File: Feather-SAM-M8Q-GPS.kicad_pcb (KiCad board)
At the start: 2 copper layers, 50.8 x 22.9 mm, 37 parts, among them U1 ublox_SAM-M8Q

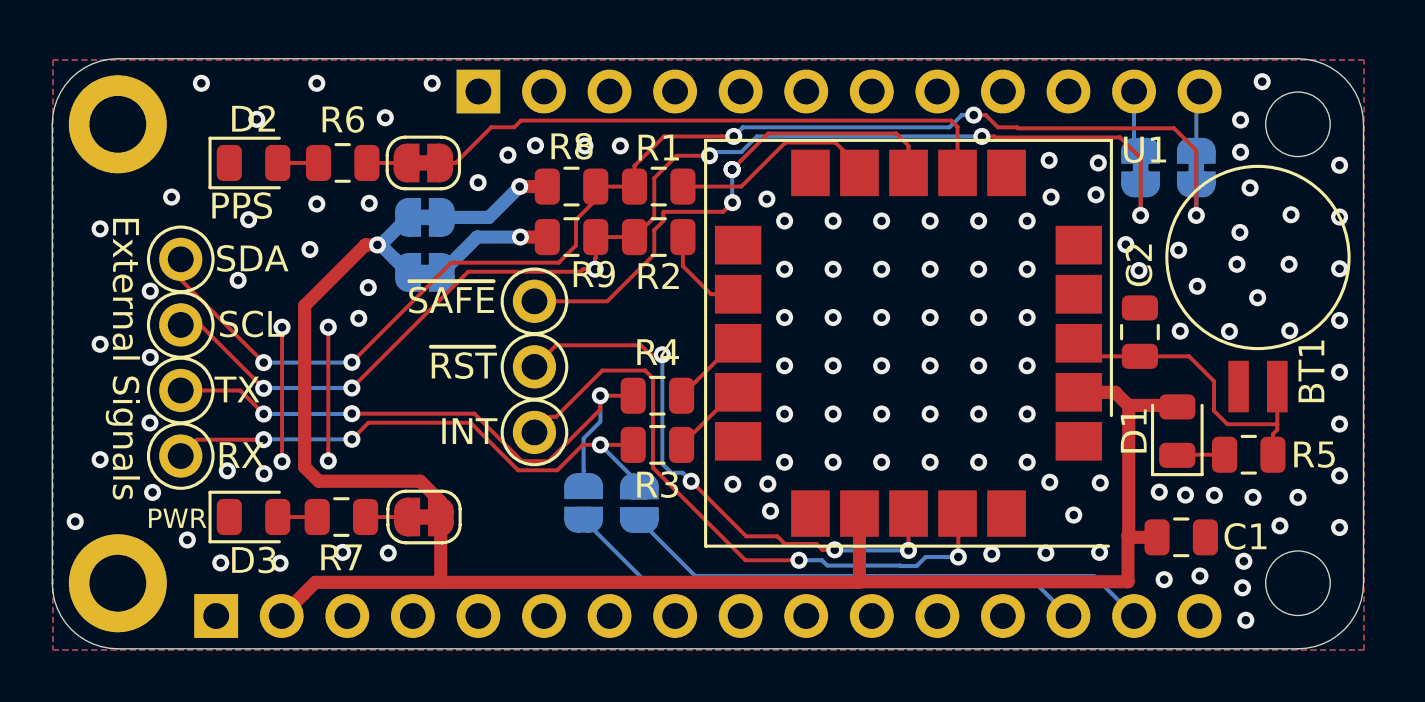
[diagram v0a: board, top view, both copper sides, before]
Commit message: Rev1.5 of SAM-M8Q GPS
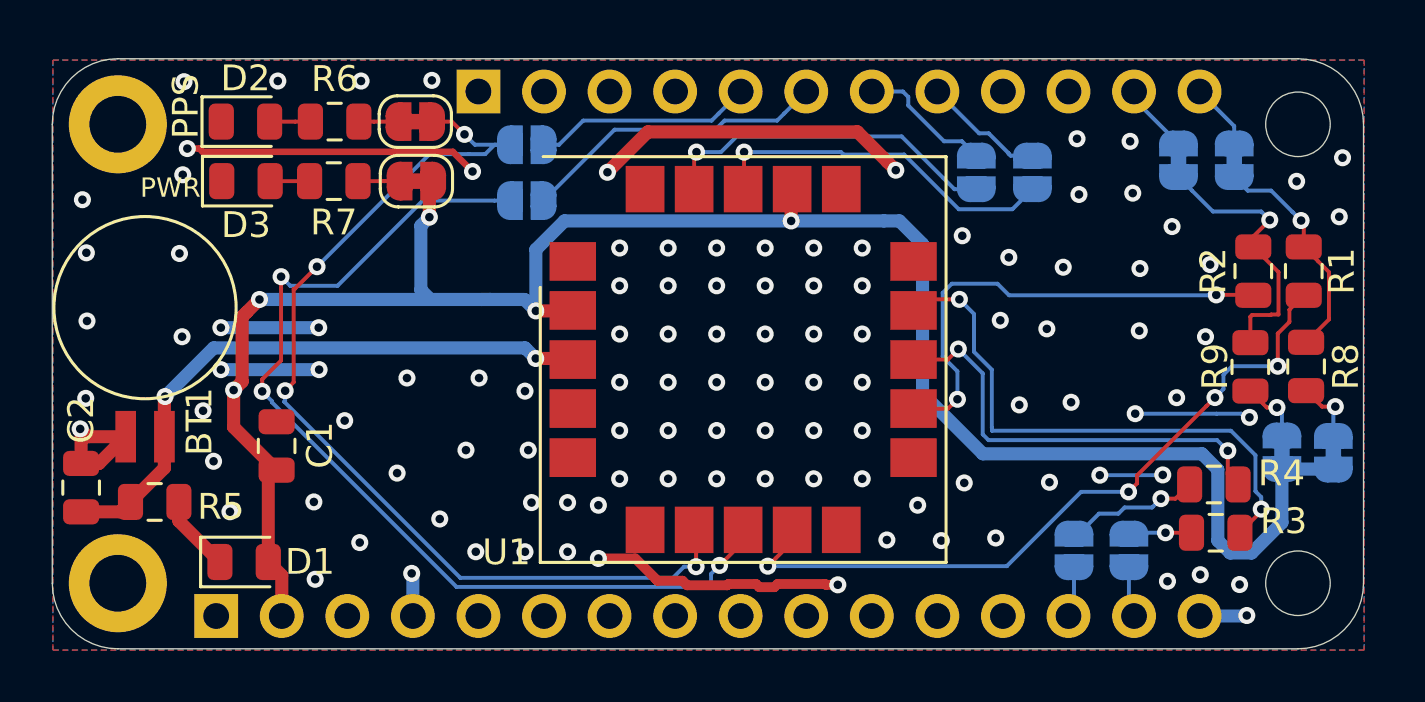
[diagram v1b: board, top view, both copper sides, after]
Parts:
- removed RX1: RX, Connector_Pin:Pin_D1.0mm_L10.0mm
- removed RX2: SCL, Connector_Pin:Pin_D1.0mm_L10.0mm
- removed RX3: INT, Connector_Pin:Pin_D1.0mm_L10.0mm
- removed TX1: TX, Connector_Pin:Pin_D1.0mm_L10.0mm
- removed TX2: SDA, Connector_Pin:Pin_D1.0mm_L10.0mm
- removed TX3: ~SAFE, Connector_Pin:Pin_D1.0mm_L10.0mm
- removed TX4: ~RST, Connector_Pin:Pin_D1.0mm_L10.0mm
- added JP10: ~, Jumper:SolderJumper-2_P1.3mm_Open_RoundedPad1.0x1.5mm, B.Cu at (122.1, 60.2)
- added JP11: ~, Jumper:SolderJumper-2_P1.3mm_Open_RoundedPad1.0x1.5mm, B.Cu at (124.3, 60.2)
- added JP12: ~, Jumper:SolderJumper-2_P1.3mm_Open_RoundedPad1.0x1.5mm, B.Cu at (104.7, 59.2)
- added JP9: ~, Jumper:SolderJumper-2_P1.3mm_Open_RoundedPad1.0x1.5mm, B.Cu at (104.7, 61.3)
- moved BT1 43.2 mm to (89.9, 70.5)
- moved R5 42.4 mm to (90.3, 73.0), turned to 0 degrees
- moved C2 41.5 mm to (87.5, 72.4)
- moved D1 36.5 mm to (93.8, 75.3), turned to 0 degrees
- moved JP3 36.4 mm to (136.0, 71.1), turned to 270 degrees
- moved C1 35.2 mm to (95.0, 70.8), turned to 90 degrees
- moved JP6 33.9 mm to (134.0, 71.1), turned to 270 degrees
- moved R8 29.3 mm to (134.9, 67.8), turned to 90 degrees
- moved R9 26.8 mm to (132.8, 67.8), turned to 90 degrees
- moved R1 25.2 mm to (134.8, 64.1), turned to 270 degrees
- moved R2 23.1 mm to (132.9, 64.1), turned to 270 degrees
- moved R3 21.9 mm to (131.4, 74.2)
- moved R4 21.8 mm to (131.3, 72.3)
- moved JP5 19.1 mm to (125.9, 74.9)
- moved JP4 19.1 mm to (128.0, 74.9)
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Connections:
- net /SCL2 renamed Net-(JP8-Pad1)
- net /SDA2 renamed Net-(JP7-Pad1)
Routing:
- net GND: track 10.4 -> 57.1 mm, vias 122 -> 113
- net Net-(JP7-Pad1): track 51.1 -> 8.91 mm, vias 5 -> 1
- net Net-(JP8-Pad1): track 47.7 -> 10.7 mm, vias 6 -> 1
- net Net-(R1-Pad2): track 8.18 -> 28.5 mm, vias 0 -> 4
- net /RX: track 21.8 -> 2.44 mm, vias 3 -> 1
- net /TXO: track 20.7 -> 1.97 mm
- net /TX: track 23.8 -> 5.11 mm, vias 3 -> 1
- net Net-(R3-Pad2): track 3.04 -> 21.6 mm, vias 0 -> 2
- net /~SAFE: track 19.9 -> 38.4 mm
- net /RXI: track 20.3 -> 1.98 mm
- net /PPS: track 22.6 -> 39.0 mm, vias 0 -> 4
- net Net-(R2-Pad2): track 3.72 -> 18.7 mm, vias 0 -> 2
- net Net-(R4-Pad2): track 3.03 -> 16.9 mm, vias 0 -> 2
- net /11`: track 0.00 -> 11.9 mm
- net /INT: track 24.4 -> 13.5 mm, vias 2 -> 1
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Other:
- board text added: "Rev2.0 ABW 1/22/20"
- board text removed: "External Signals"
- board text removed: "RX"
- board text removed: "Rev1.5 ABW 12/30/19"
- board text removed: "SCL"
- board text removed: "SDA"
- board text removed: "TX"
